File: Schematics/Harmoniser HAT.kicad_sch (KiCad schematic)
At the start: 0 parts

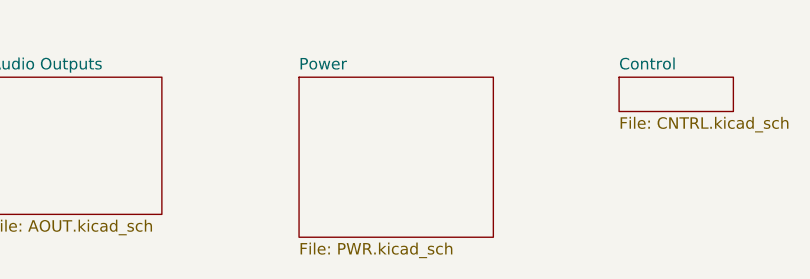
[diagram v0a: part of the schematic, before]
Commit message: Input Buffer & EEPROM
line and instrument level buffers for the input added. EEPROM added and credits attributed !
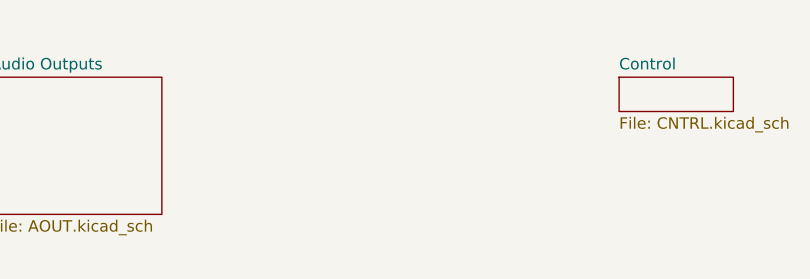
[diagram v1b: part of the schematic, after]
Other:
- removed sheet Power
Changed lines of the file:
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@@
-	)
-	(sheet
-		(at 172.72 34.29)
-		(size 21.59 17.78)
-		(fields_autoplaced yes)
-		(stroke
-			(width 0.1524)
-			(type solid)
-		)
-		(fill
-			(color 0 0 0 0.0000)
-		)
-		(property "Sheetname" "Power"
-			(at 172.72 33.5784 0)
-			(effects
-				(font
-					(size 1.27 1.27)
-				)
-				(justify left bottom)
-			)
-		)
-		(property "Sheetfile" "PWR.kicad_sch"
-			(at 172.72 52.6546 0)
-			(effects
-				(font
-					(size 1.27 1.27)
-				)
-				(justify left top)
-			)
-		)
-		(instances
-			(project "Harmoniser HAT"
-				(path "/41751dd2-97f9-4cc6-b9e6-b561e5949053"
-					(page "6")
-				)
-			)
-		)
 	)
 	(sheet

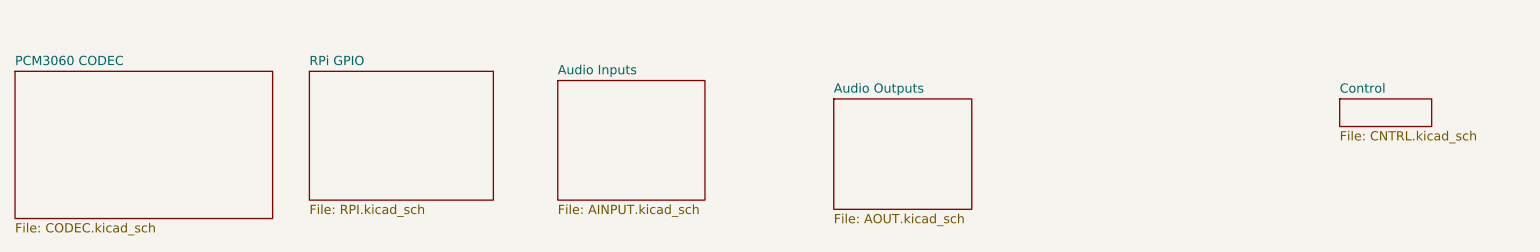
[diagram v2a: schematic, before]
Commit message: Added Debug Headers
Added debug headers for I2C, I2S, and power. Also added m2.5 mounting holes for hat
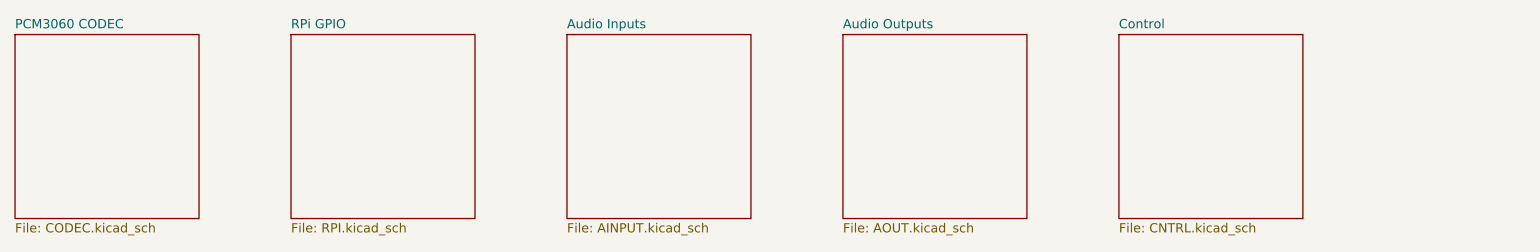
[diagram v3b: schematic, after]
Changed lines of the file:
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@@
 	(paper "A4")
 	(sheet
-		(at 25.4 30.48)
-		(size 35.56 20.32)
+		(at 25.4 25.4)
+		(size 25.4 25.4)
 		(fields_autoplaced yes)
 		(stroke
@@
 		)
 		(property "Sheetname" "PCM3060 CODEC"
-			(at 25.4 29.7684 0)
+			(at 25.4 24.6884 0)
 			(effects
 				(font
@@
 	)
 	(sheet
-		(at 100.33 31.75)
-		(size 20.32 16.51)
+		(at 101.6 25.4)
+		(size 25.4 25.4)
 		(fields_autoplaced yes)
 		(stroke
@@
 		)
 		(property "Sheetname" "Audio Inputs"
-			(at 100.33 31.0384 0)
+			(at 101.6 24.6884 0)
 			(effects
 				(font
@@
 		)
 		(property "Sheetfile" "AINPUT.kicad_sch"
-			(at 100.33 48.8446 0)
+			(at 101.6 51.3846 0)
 			(effects
 				(font
@@
 	)
 	(sheet
-		(at 208.28 34.29)
-		(size 12.7 3.81)
+		(at 177.8 25.4)
+		(size 25.4 25.4)
 		(fields_autoplaced yes)
 		(stroke
@@
 		)
 		(property "Sheetname" "Control"
-			(at 208.28 33.5784 0)
+			(at 177.8 24.6884 0)
 			(effects
 				(font
@@
 		)
 		(property "Sheetfile" "CNTRL.kicad_sch"
-			(at 208.28 38.6846 0)
+			(at 177.8 51.3846 0)
 			(effects
 				(font
@@
 	)
 	(sheet
-		(at 66.04 30.48)
-		(size 25.4 17.78)
+		(at 63.5 25.4)
+		(size 25.4 25.4)
 		(fields_autoplaced yes)
 		(stroke
@@
 		)
 		(property "Sheetname" "RPi GPIO"
-			(at 66.04 29.7684 0)
+			(at 63.5 24.6884 0)
 			(effects
 				(font
@@
 		)
 		(property "Sheetfile" "RPI.kicad_sch"
-			(at 66.04 48.8446 0)
+			(at 63.5 51.3846 0)
 			(effects
 				(font
@@
 	)
 	(sheet
-		(at 138.43 34.29)
-		(size 19.05 15.24)
+		(at 139.7 25.4)
+		(size 25.4 25.4)
 		(fields_autoplaced yes)
 		(stroke
@@
 		)
 		(property "Sheetname" "Audio Outputs"
-			(at 138.43 33.5784 0)
+			(at 139.7 24.6884 0)
 			(effects
 				(font
@@
 		)
 		(property "Sheetfile" "AOUT.kicad_sch"
-			(at 138.43 50.1146 0)
+			(at 139.7 51.3846 0)
 			(effects
 				(font

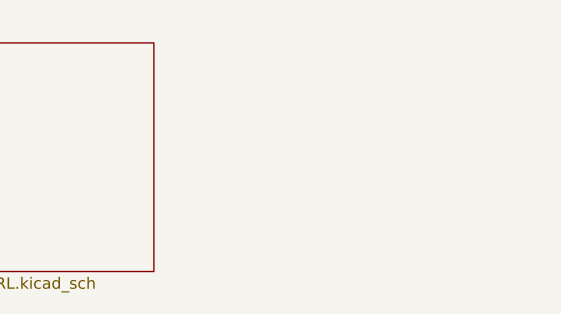
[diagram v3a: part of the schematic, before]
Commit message: Started adding footprints, changed values.
Added footprints for most components. need to check in uni which sizes are available and what will need to be ordered from mouser.
Changed line in/out to TRS as this will be more reliable and added 0 ohm resistor options to bypass mono input and use line in/out as stereo.
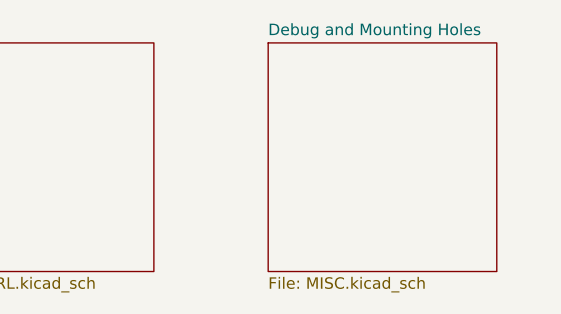
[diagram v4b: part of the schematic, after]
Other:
- added sheet Debug and Mounting Holes (MISC.kicad_sch)
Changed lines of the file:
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@@
 	(paper "A4")
+	(sheet
+		(at 215.9 25.4)
+		(size 25.4 25.4)
+		(fields_autoplaced yes)
+		(stroke
+			(width 0.1524)
+			(type solid)
+		)
+		(fill
+			(color 0 0 0 0.0000)
+		)
+		(property "Sheetname" "Debug and Mounting Holes"
+			(at 215.9 24.6884 0)
+			(effects
+				(font
+					(size 1.27 1.27)
+				)
+				(justify left bottom)
+			)
+		)
+		(property "Sheetfile" "MISC.kicad_sch"
+			(at 215.9 51.3846 0)
+			(effects
+				(font
+					(size 1.27 1.27)
+				)
+				(justify left top)
+			)
+		)
+		(instances
+			(project "Harmoniser HAT"
+				(path "/41751dd2-97f9-4cc6-b9e6-b561e5949053"
+					(page "7")
+				)
+			)
+		)
+	)
 	(sheet
 		(at 25.4 25.4)
@@
 			(project "Harmoniser HAT"
 				(path "/41751dd2-97f9-4cc6-b9e6-b561e5949053"
-					(page "7")
+					(page "6")
 				)
 			)

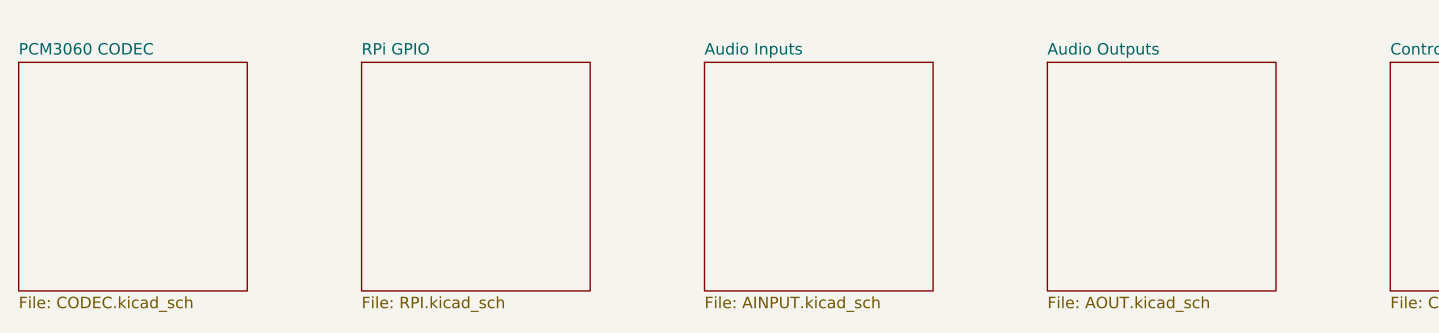
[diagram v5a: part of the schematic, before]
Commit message: Fix for Uni PCB
CODEC module, DIP package, and through-hole less components
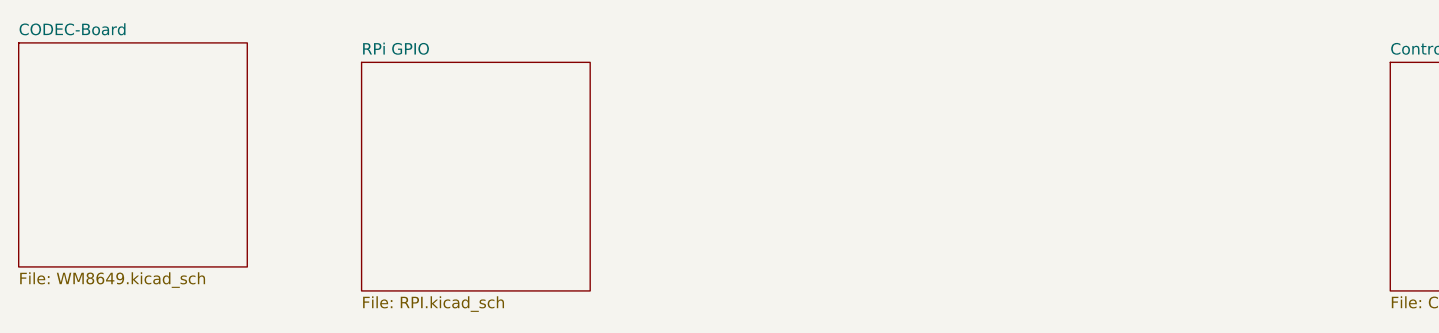
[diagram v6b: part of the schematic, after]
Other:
- removed sheet Audio Inputs
- removed sheet Audio Outputs
- removed sheet PCM3060 CODEC
- added sheet CODEC-Board (WM8649.kicad_sch)
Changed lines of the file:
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@@
-	)
-	(sheet
-		(at 25.4 25.4)
-		(size 25.4 25.4)
-		(exclude_from_sim no)
-		(in_bom yes)
-		(on_board yes)
-		(dnp no)
-		(fields_autoplaced yes)
-		(stroke
-			(width 0.1524)
-			(type solid)
-		)
-		(fill
-			(color 0 0 0 0.0000)
-		)
-		(property "Sheetname" "PCM3060 CODEC"
-			(at 25.4 24.6884 0)
-			(effects
-				(font
-					(size 1.27 1.27)
-				)
-				(justify left bottom)
-			)
-		)
-		(property "Sheetfile" "CODEC.kicad_sch"
-			(at 25.4 51.3846 0)
-			(effects
-				(font
-					(size 1.27 1.27)
-				)
-				(justify left top)
-			)
-		)
-		(instances
-			(project "Harmoniser HAT"
-				(path "/41751dd2-97f9-4cc6-b9e6-b561e5949053"
-					(page "2")
-				)
-			)
-		)
-	)
-	(sheet
-		(at 101.6 25.4)
-		(size 25.4 25.4)
-		(exclude_from_sim no)
-		(in_bom yes)
-		(on_board yes)
-		(dnp no)
-		(fields_autoplaced yes)
-		(stroke
-			(width 0.1524)
-			(type solid)
-		)
-		(fill
-			(color 0 0 0 0.0000)
-		)
-		(property "Sheetname" "Audio Inputs"
-			(at 101.6 24.6884 0)
-			(effects
-				(font
-					(size 1.27 1.27)
-				)
-				(justify left bottom)
-			)
-		)
-		(property "Sheetfile" "AINPUT.kicad_sch"
-			(at 101.6 51.3846 0)
-			(effects
-				(font
-					(size 1.27 1.27)
-				)
-				(justify left top)
-			)
-		)
-		(instances
-			(project "Harmoniser HAT"
-				(path "/41751dd2-97f9-4cc6-b9e6-b561e5949053"
-					(page "4")
-				)
-			)
-		)
 	)
 	(sheet
@@
 	)
 	(sheet
-		(at 139.7 25.4)
-		(size 25.4 25.4)
+		(at 25.4 23.241)
+		(size 25.4 24.892)
 		(exclude_from_sim no)
 		(in_bom yes)
@@
 			(color 0 0 0 0.0000)
 		)
-		(property "Sheetname" "Audio Outputs"
-			(at 139.7 24.6884 0)
+		(property "Sheetname" "CODEC-Board"
+			(at 25.4 22.5294 0)
 			(effects
 				(font
@@
 			)
 		)
-		(property "Sheetfile" "AOUT.kicad_sch"
-			(at 139.7 51.3846 0)
+		(property "Sheetfile" "WM8649.kicad_sch"
+			(at 25.4 48.7176 0)
 			(effects
 				(font
@@
 			(project "Harmoniser HAT"
 				(path "/41751dd2-97f9-4cc6-b9e6-b561e5949053"
-					(page "5")
+					(page "8")
 				)
 			)

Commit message: Tidied up Schematic
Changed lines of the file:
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@@
 	(paper "A4")
 	(sheet
-		(at 215.9 25.4)
+		(at 63.5 63.5)
 		(size 25.4 25.4)
 		(exclude_from_sim no)
@@
 		)
 		(property "Sheetname" "Debug and Mounting Holes"
-			(at 215.9 24.6884 0)
+			(at 63.5 62.7884 0)
 			(effects
 				(font
@@
 		)
 		(property "Sheetfile" "MISC.kicad_sch"
-			(at 215.9 51.3846 0)
+			(at 63.5 89.4846 0)
 			(effects
 				(font
@@
 	)
 	(sheet
-		(at 177.8 25.4)
+		(at 25.4 63.5)
 		(size 25.4 25.4)
 		(exclude_from_sim no)
@@
 		)
 		(property "Sheetname" "Control"
-			(at 177.8 24.6884 0)
+			(at 25.4 62.7884 0)
 			(effects
 				(font
@@
 		)
 		(property "Sheetfile" "CNTRL.kicad_sch"
-			(at 177.8 51.3846 0)
+			(at 25.4 89.4846 0)
 			(effects
 				(font
@@
 	)
 	(sheet
-		(at 63.5 25.4)
+		(at 25.4 25.4)
 		(size 25.4 25.4)
 		(exclude_from_sim no)
@@
 		)
 		(property "Sheetname" "RPi GPIO"
-			(at 63.5 24.6884 0)
+			(at 25.4 24.6884 0)
 			(effects
 				(font
@@
 		)
 		(property "Sheetfile" "RPI.kicad_sch"
-			(at 63.5 51.3846 0)
+			(at 25.4 51.3846 0)
 			(effects
 				(font
@@
 	)
 	(sheet
-		(at 25.4 23.241)
+		(at 63.5 25.781)
 		(size 25.4 24.892)
 		(exclude_from_sim no)
@@
 		)
 		(property "Sheetname" "CODEC-Board"
-			(at 25.4 22.5294 0)
+			(at 63.5 25.0694 0)
 			(effects
 				(font
@@
 		)
 		(property "Sheetfile" "WM8649.kicad_sch"
-			(at 25.4 48.7176 0)
+			(at 63.5 51.2576 0)
 			(effects
 				(font
